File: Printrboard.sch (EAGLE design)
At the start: 122 parts, among them J1 MICROSD, J3 ATX, Q1 RFP30N06LE, Q2 RFP30N06LE, Q3 RFP30N06LE, U1 LM2841, U2 A4982, U3 A4982, U4 A4982, U5 A4982, U6 AT90USB1286, U7 AP7313, U8 TXB0104, X1 16MHz, X2 USB-MICROB

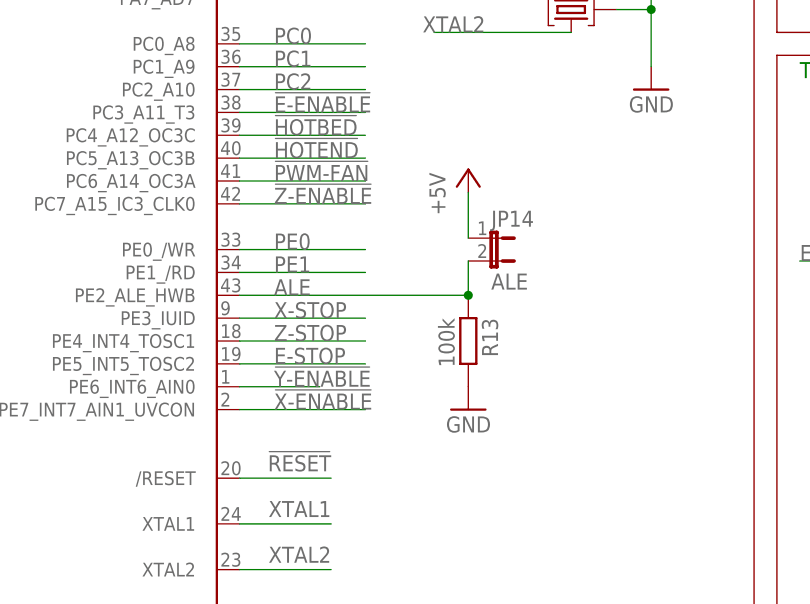
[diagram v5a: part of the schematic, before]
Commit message: Make resonator pad larger to accomodate both available pacakages, and change polarity of BOOT jumper
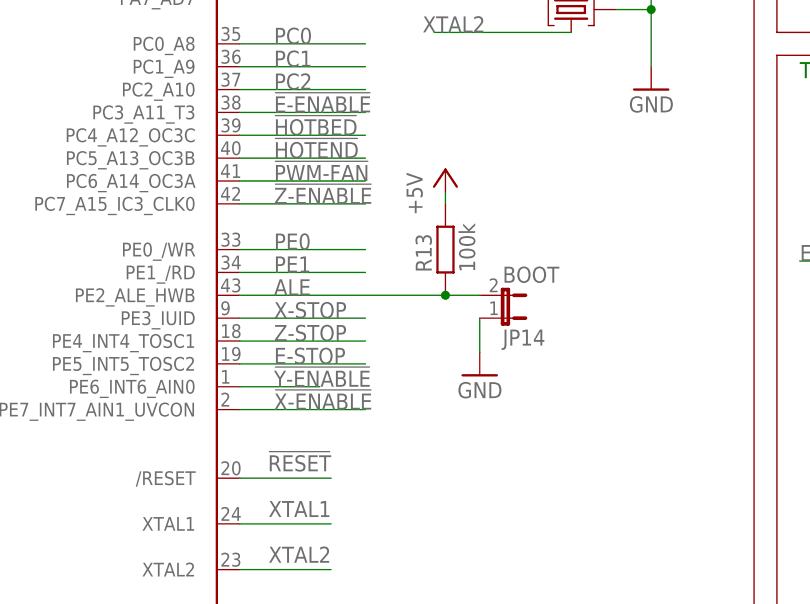
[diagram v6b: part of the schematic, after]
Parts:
- JP14: value ALE -> BOOT
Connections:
- net +5V: now also R13.2; no longer JP14.1
- net GND: now also JP14.1; no longer R13.2
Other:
- moved on the sheet: JP14, R13
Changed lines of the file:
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@@
 <setting verticaltext="up"/>
 </settings>
-<grid distance="0.1" unitdist="inch" unit="inch" style="lines" multiple="1" display="no" altdistance="0.01" altunitdist="inch" altunit="inch"/>
+<grid distance="0.1" unitdist="inch" unit="inch" style="lines" multiple="1" display="no" altdistance="0.05" altunitdist="inch" altunit="inch"/>
 <layers>
 <layer number="1" name="Top" color="4" fill="1" visible="no" active="no"/>
@@
 <part name="GND39" library="supply1" deviceset="GND" device=""/>
 <part name="C13" library="ipc-7351-capacitor" deviceset="CAPACITOR_" device="0805" value="0.1uF"/>
-<part name="GND7" library="SparkFun" deviceset="GND" device=""/>
 <part name="R12" library="ipc-7351-resistor" deviceset="RESISTOR_" device="0805" value="100k"/>
 <part name="GND10" library="SparkFun" deviceset="GND" device=""/>
@@
 <part name="JP17" library="SparkFun" deviceset="M02" device="PTH" value="FAN"/>
 <part name="U$38" library="12v" deviceset="12V" device=""/>
-<part name="JP14" library="SparkFun" deviceset="JUMPER-2" device="PTH" value="ALE"/>
+<part name="JP14" library="SparkFun" deviceset="JUMPER-2" device="PTH" value="BOOT"/>
 <part name="R1" library="ipc-7351-resistor" deviceset="RESISTOR_" device="0805" value="330"/>
 <part name="LED2" library="led" deviceset="LED" device="CHIP-LED0805" value="PWR"/>
@@
 <part name="P+19" library="supply1" deviceset="+5V" device=""/>
 <part name="S1" library="printrbot" deviceset="SWITCH-MOMENTARY-2" device="" value="Reset"/>
+<part name="GND7" library="SparkFun" deviceset="GND" device=""/>
 </parts>
 <sheets>
@@
 <instance part="GND39" gate="1" x="233.68" y="106.68"/>
 <instance part="C13" gate="G$1" x="25.4" y="111.76" rot="MR90"/>
-<instance part="GND7" gate="1" x="161.29" y="49.53" rot="MR0"/>
 <instance part="R12" gate="G$1" x="166.37" y="110.49" rot="MR90"/>
 <instance part="GND10" gate="1" x="24.13" y="40.64"/>
@@
 <attribute name="VALUE" x="52.07" y="34.29" size="1.778" layer="96"/>
 </instance>
-<instance part="R13" gate="G$1" x="161.29" y="57.15" rot="R270"/>
+<instance part="R13" gate="G$1" x="158.75" y="67.31" rot="R90"/>
 <instance part="JP13" gate="G$1" x="223.52" y="144.78" rot="R180"/>
 <instance part="C9" gate="G$1" x="210.82" y="20.32" rot="R90"/>
@@
 <instance part="JP17" gate="G$1" x="63.5" y="226.06" rot="R180"/>
 <instance part="U$38" gate="G$1" x="53.34" y="228.6"/>
-<instance part="JP14" gate="A" x="163.83" y="68.58" rot="R270"/>
+<instance part="JP14" gate="A" x="165.1" y="59.69" rot="MR90"/>
 <instance part="R1" gate="G$1" x="222.25" y="-22.86" rot="R90"/>
 <instance part="LED2" gate="G$1" x="222.25" y="-33.02"/>
@@
 </instance>
 <instance part="P+5" gate="1" x="166.37" y="120.65"/>
-<instance part="P+6" gate="1" x="161.29" y="76.2"/>
+<instance part="P+6" gate="1" x="158.75" y="76.2"/>
 <instance part="P+7" gate="1" x="213.36" y="81.28"/>
 <instance part="P+8" gate="1" x="213.36" y="40.64"/>
@@
 <instance part="P+19" gate="1" x="31.75" y="78.74"/>
 <instance part="S1" gate="G$1" x="176.53" y="109.22"/>
+<instance part="GND7" gate="1" x="162.56" y="53.34" rot="MR0"/>
 </instances>
 <busses>
@@
 <pinref part="GND5" gate="1" pin="GND"/>
 <pinref part="C13" gate="G$1" pin="1"/>
-</segment>
-<segment>
-<pinref part="GND7" gate="1" pin="GND"/>
-<pinref part="R13" gate="G$1" pin="2"/>
 </segment>
 <segment>
@@
 <pinref part="C36" gate="G$1" pin="1"/>
 </segment>
+<segment>
+<pinref part="GND7" gate="1" pin="GND"/>
+<pinref part="JP14" gate="A" pin="1"/>
+<wire x1="162.56" y1="55.88" x2="162.56" y2="59.69" width="0.1524" layer="91"/>
+</segment>
 </net>
 <net name="!RESET" class="0">
@@
 <net name="ALE" class="0">
 <segment>
-<wire x1="161.29" y1="62.23" x2="135.89" y2="62.23" width="0.1524" layer="91"/>
+<wire x1="158.75" y1="62.23" x2="135.89" y2="62.23" width="0.1524" layer="91"/>
 <label x="139.7" y="62.23" size="1.778" layer="95"/>
 <pinref part="R13" gate="G$1" pin="1"/>
 <pinref part="U6" gate="G$1" pin="PE2_ALE_HWB"/>
 <pinref part="JP14" gate="A" pin="2"/>
-<wire x1="161.29" y1="66.04" x2="161.29" y2="62.23" width="0.1524" layer="91"/>
-<junction x="161.29" y="62.23"/>
+<wire x1="162.56" y1="62.23" x2="158.75" y2="62.23" width="0.1524" layer="91"/>
+<junction x="158.75" y="62.23"/>
 </segment>
 </net>
@@
 </segment>
 <segment>
-<wire x1="161.29" y1="68.58" x2="161.29" y2="73.66" width="0.1524" layer="91"/>
-<pinref part="JP14" gate="A" pin="1"/>
-<pinref part="P+6" gate="1" pin="+5V"/>
-</segment>
-<segment>
 <wire x1="213.36" y1="78.74" x2="213.36" y2="76.2" width="0.1524" layer="91"/>
 <pinref part="R9" gate="G$1" pin="2"/>
@@
 <wire x1="31.75" y1="69.85" x2="31.75" y2="76.2" width="0.1524" layer="91"/>
 </segment>
-</net>
+<segment>
+<pinref part="P+6" gate="1" pin="+5V"/>
+<pinref part="R13" gate="G$1" pin="2"/>
+<wire x1="158.75" y1="73.66" x2="158.75" y2="72.39" width="0.1524" layer="91"/>
+</segment>
+</net>

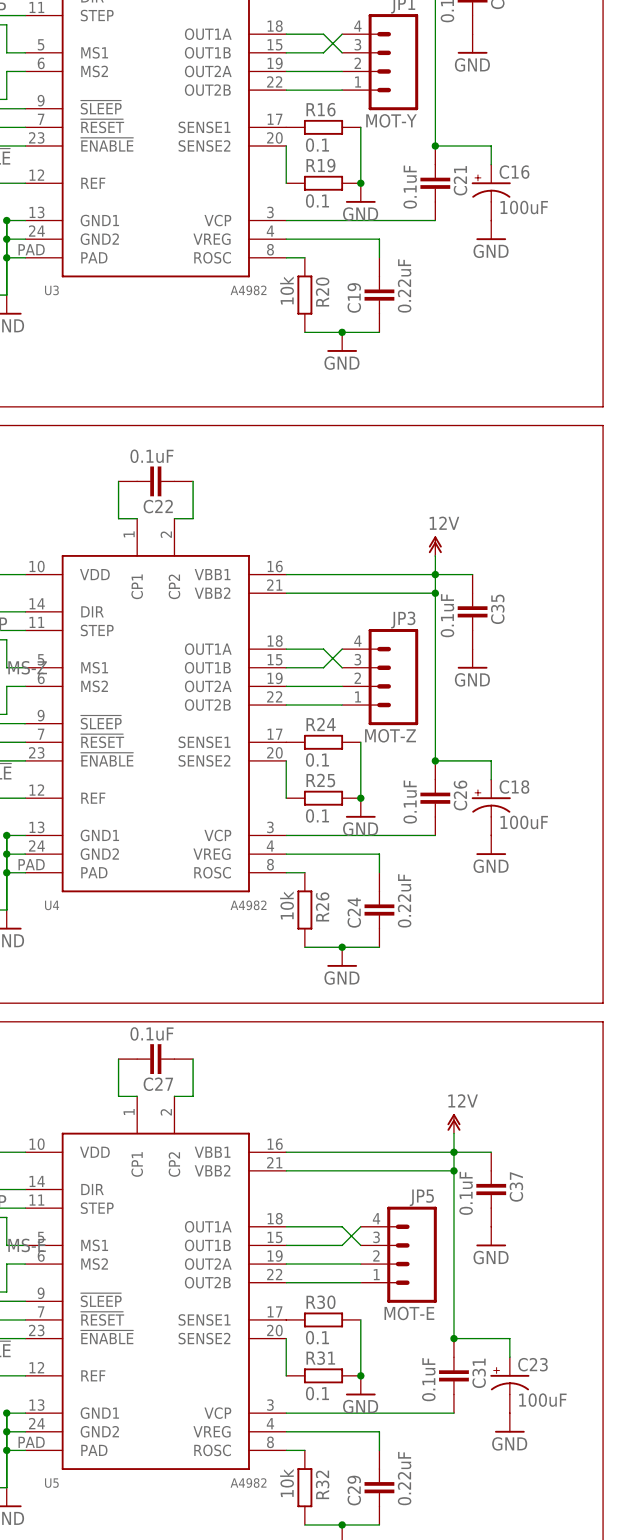
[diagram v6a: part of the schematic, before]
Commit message: Fix values for sense resistors to match BoM
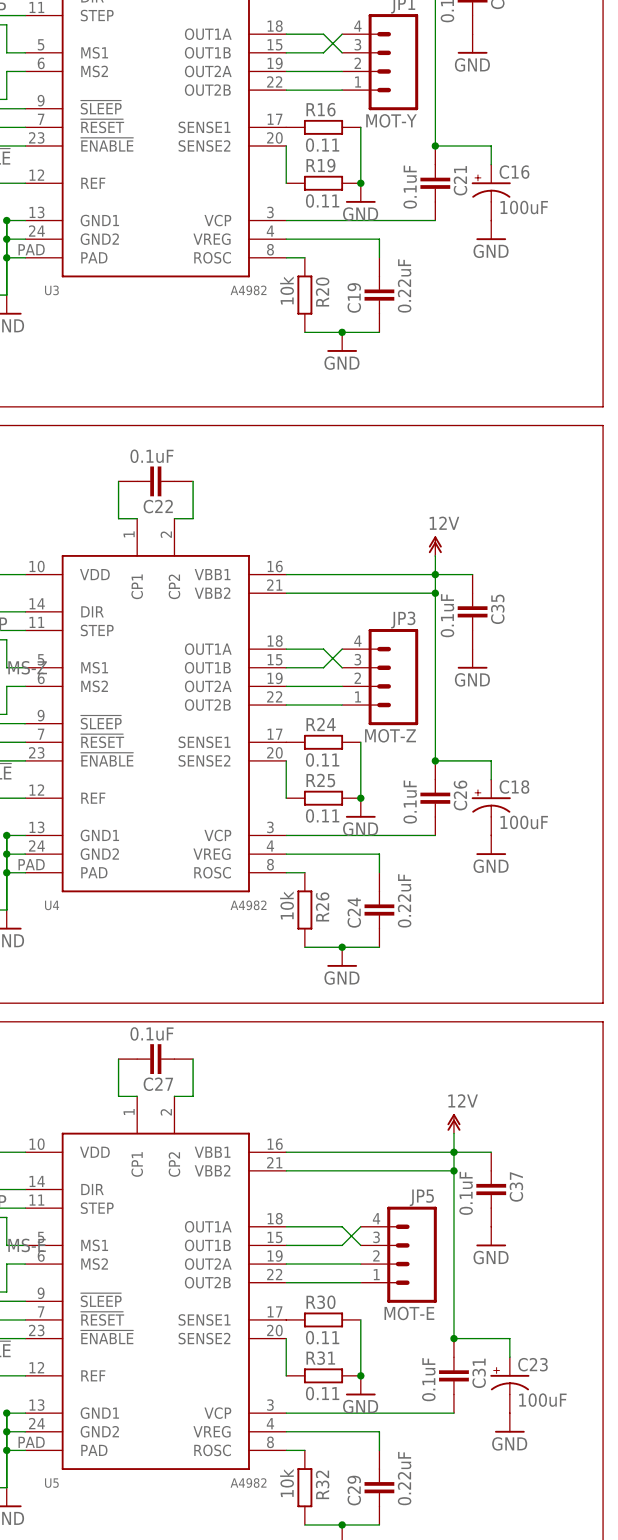
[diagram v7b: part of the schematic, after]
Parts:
- R16, R19, R24, R25, R30, R31: value 0.1 -> 0.11
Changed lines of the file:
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@@
 <part name="GND8" library="SparkFun" deviceset="GND" device=""/>
 <part name="U$2" library="12v" deviceset="12V" device=""/>
-<part name="R16" library="ipc-7351-resistor" deviceset="RESISTOR_" device="0805" value="0.1"/>
-<part name="R19" library="ipc-7351-resistor" deviceset="RESISTOR_" device="0805" value="0.1"/>
+<part name="R16" library="ipc-7351-resistor" deviceset="RESISTOR_" device="0805" value="0.11"/>
+<part name="R19" library="ipc-7351-resistor" deviceset="RESISTOR_" device="0805" value="0.11"/>
 <part name="GND11" library="SparkFun" deviceset="GND" device=""/>
 <part name="C19" library="ipc-7351-capacitor" deviceset="CAPACITOR_" device="0805" value="0.22uF"/>
@@
 <part name="GND32" library="SparkFun" deviceset="GND" device=""/>
 <part name="U$3" library="12v" deviceset="12V" device=""/>
-<part name="R24" library="ipc-7351-resistor" deviceset="RESISTOR_" device="0805" value="0.1"/>
-<part name="R25" library="ipc-7351-resistor" deviceset="RESISTOR_" device="0805" value="0.1"/>
+<part name="R24" library="ipc-7351-resistor" deviceset="RESISTOR_" device="0805" value="0.11"/>
+<part name="R25" library="ipc-7351-resistor" deviceset="RESISTOR_" device="0805" value="0.11"/>
 <part name="GND33" library="SparkFun" deviceset="GND" device=""/>
 <part name="C24" library="ipc-7351-capacitor" deviceset="CAPACITOR_" device="0805" value="0.22uF"/>
@@
 <part name="GND41" library="SparkFun" deviceset="GND" device=""/>
 <part name="U$4" library="12v" deviceset="12V" device=""/>
-<part name="R30" library="ipc-7351-resistor" deviceset="RESISTOR_" device="0805" value="0.1"/>
-<part name="R31" library="ipc-7351-resistor" deviceset="RESISTOR_" device="0805" value="0.1"/>
+<part name="R30" library="ipc-7351-resistor" deviceset="RESISTOR_" device="0805" value="0.11"/>
+<part name="R31" library="ipc-7351-resistor" deviceset="RESISTOR_" device="0805" value="0.11"/>
 <part name="GND42" library="SparkFun" deviceset="GND" device=""/>
 <part name="C29" library="ipc-7351-capacitor" deviceset="CAPACITOR_" device="0805" value="0.22uF"/>
